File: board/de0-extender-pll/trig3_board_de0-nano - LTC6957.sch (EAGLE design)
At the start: 94 parts, among them IC1 FT230XQ, J12 4p-2.54, J13 BU-SMB-V, J17 2p-2.54, J23 2p-2.54, J24 2p-2.54, J32 2p-2.54, J34 2p-2.54, J38 2p-2.54, J42 2p-2.54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

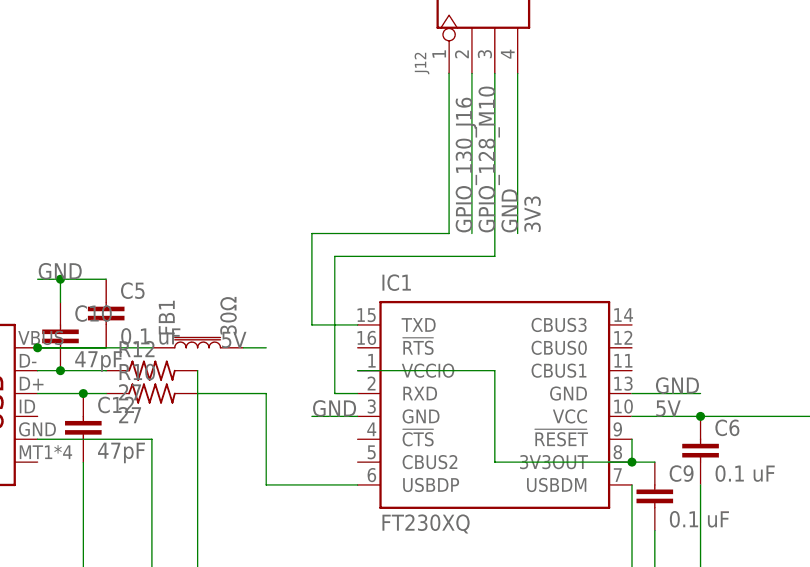
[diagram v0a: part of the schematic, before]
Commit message: rotated footprints and cosmetic updates to board
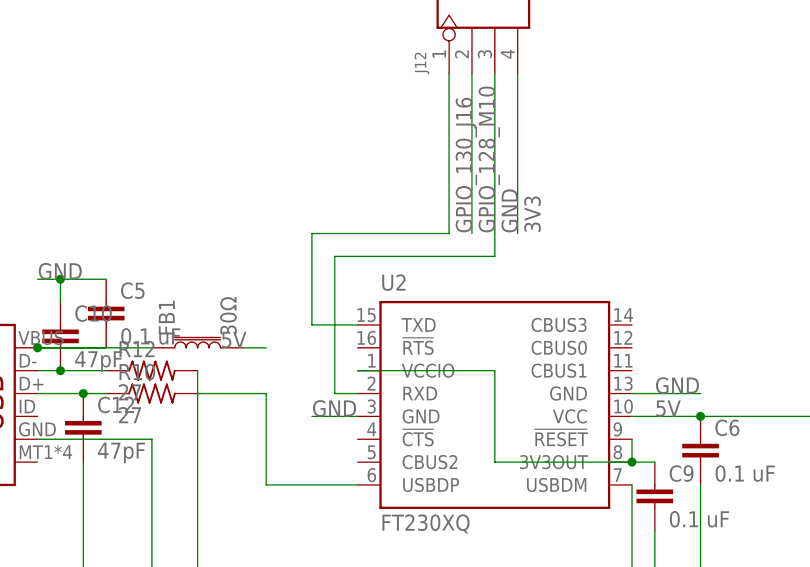
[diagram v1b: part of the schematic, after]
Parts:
- removed IC1: FT230XQ, ftdichip:FT230XQ
- added U2: FT230XQ, ftdichip-rotate-footprint-jlcpcb:FT230XQ
- renumbered VSLUE5 to U5, VSLUE7 to U4, VSLUE9 to U3
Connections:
- net 5V: now also U2.VCC; no longer IC1.VCC
- net GND: now also U2.GND, U2.GND@1, U2.RXD; no longer IC1.GND, IC1.GND@1, IC1.RXD
- net GPIO_130_J16: now also U2.TXD; no longer IC1.TXD
- net N$12: now also U2.USBDP; no longer IC1.USBDP
- net N$13: now also U2.USBDM; no longer IC1.USBDM
- net N$14: now also U2.!RESET, U2.3V3OUT, U2.VCCIO; no longer IC1.!RESET, IC1.3V3OUT, IC1.VCCIO

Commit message: ready for ordering
will probably need to do one last check
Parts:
- A6, B6, C11, C16, CLK-IN+, CLK-IN-, CLK_OUT+, CLK_OUT-, E11, E7, F9, J13, K15P, K16N, L15_R11P, L16_R11N, N11, P11, P15, P16_R15N, P9, R13P, R16_R15P, T13N: LCSC_PART# (none) -> C496549
- C13: LCSC_PART# (none) -> C19666
- J1: value (none) -> USB micro-b
- LED1: device led:LEDCHIP-LED0805 -> led:LEDSML0805
- S2: LCSC_PART# (none) -> C2842669

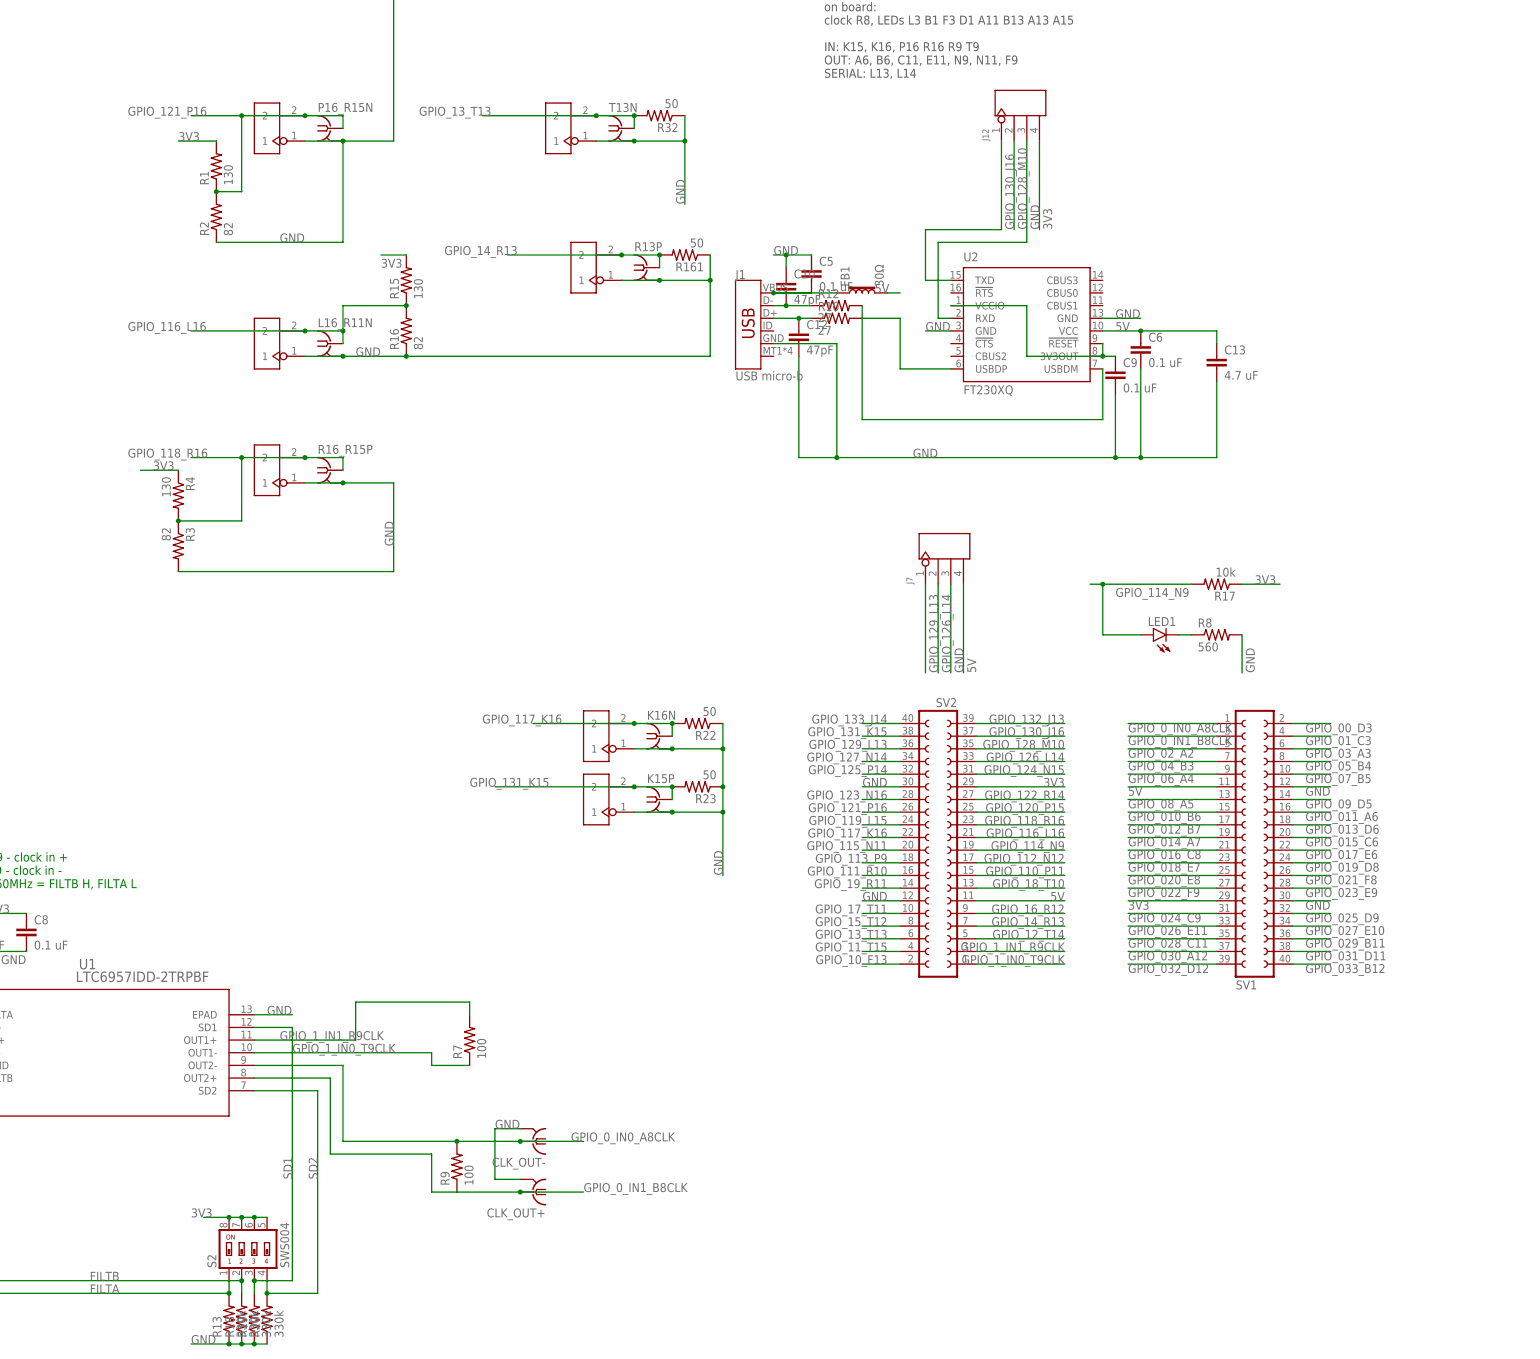
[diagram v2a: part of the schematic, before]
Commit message: fixed usb connection error; changed connector; change dip switch part
added sd1, sd2, filta, filtb to gpio pins also
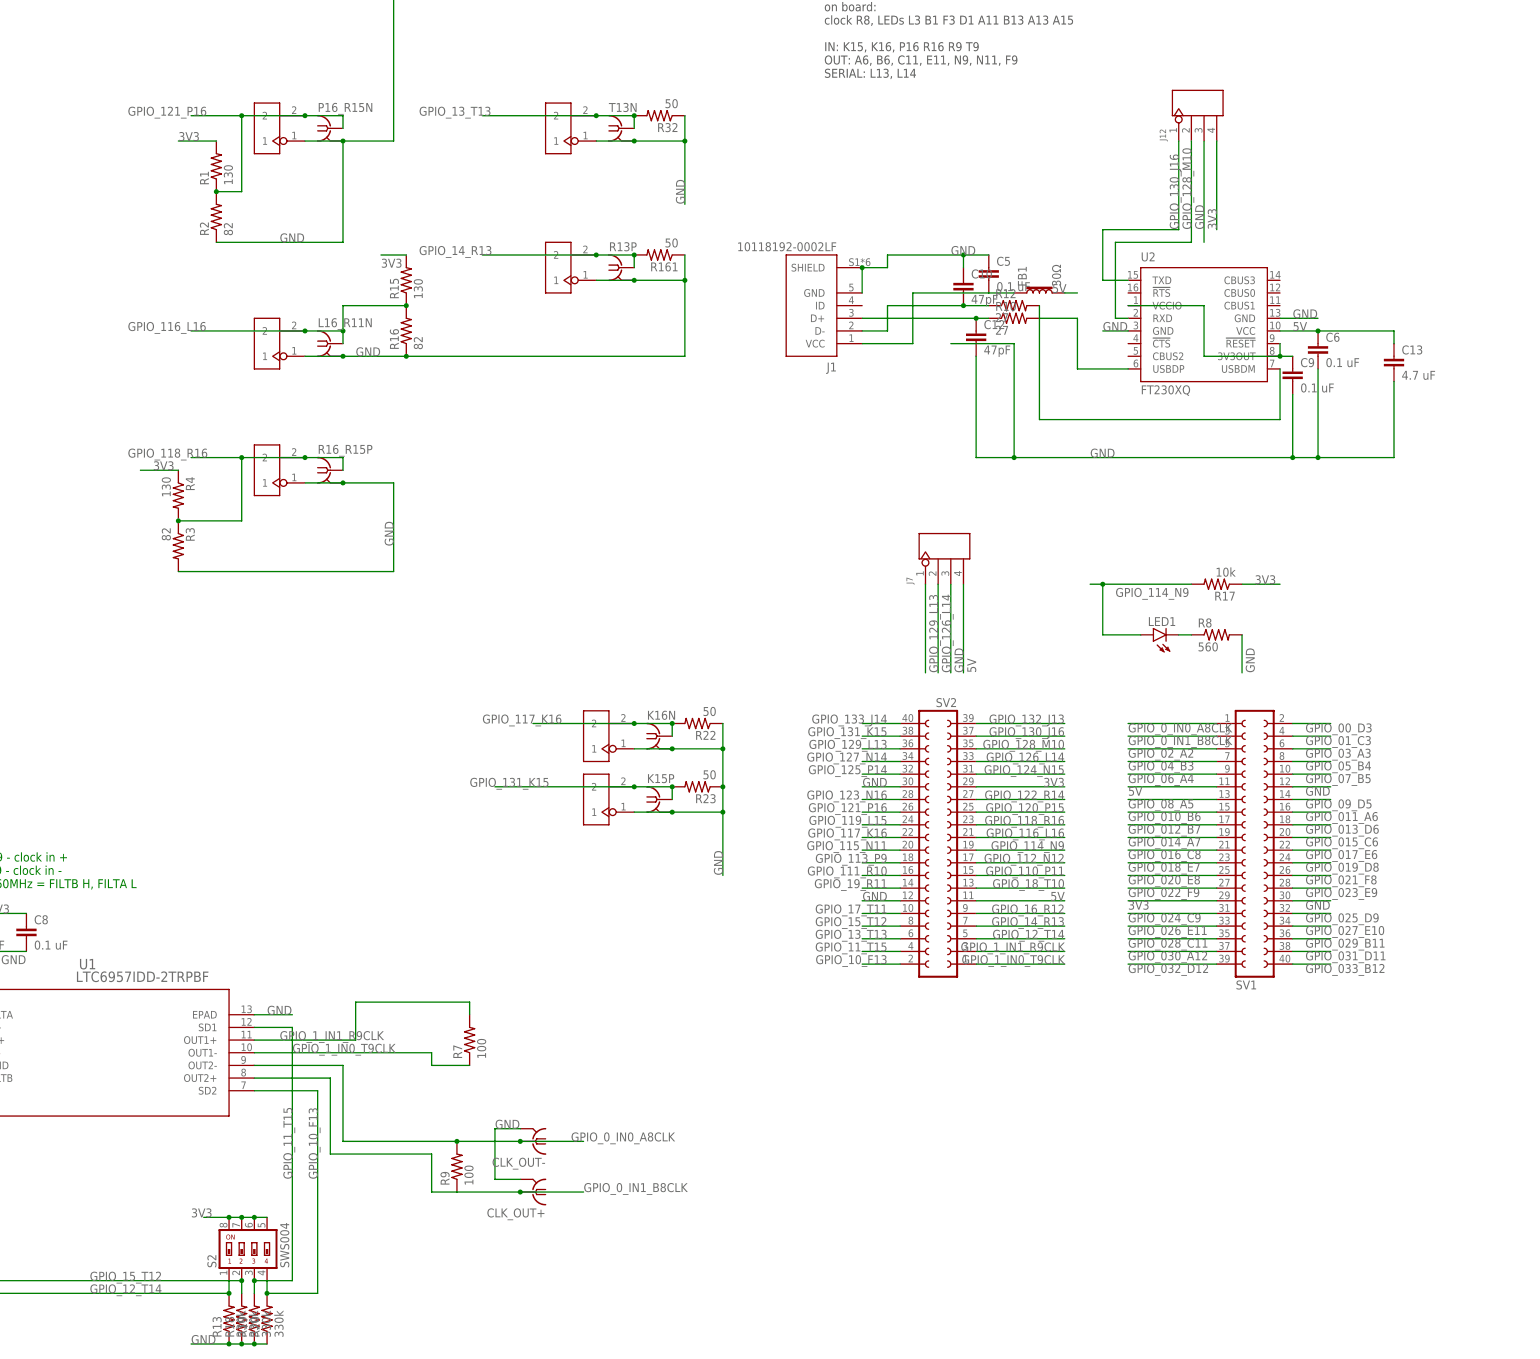
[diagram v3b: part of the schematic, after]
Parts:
- J1: value USB micro-b -> 10118192-0002LF; device SparkFun-Connectors:USB_MICRO-B_SMT -> 10118192-0002LF:10118192-0002LF; LCSC_PART# C2926993 -> C132564
- S2: LCSC_PART# C2842669 -> C221954
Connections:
- removed net FILTA: R13.2, S2.1, U1.FILTA
- removed net FILTB: R18.2, S2.2, U1.FILTB
- removed net SD1: R19.2, S2.3, U1.SD1
- removed net SD2: R20.2, S2.4, U1.SD2
- net GND: now also J1.SHIELD; no longer U2.RXD
- net GPIO_10_F13: now also R20.2, S2.4, U1.SD2
- net GPIO_11_T15: now also R19.2, S2.3, U1.SD1
- net GPIO_128_M10: now also U2.RXD
- net GPIO_12_T14: now also R13.2, S2.1, U1.FILTA
- net GPIO_15_T12: now also R18.2, S2.2, U1.FILTB
- net N$6: now also J1.VCC; no longer J1.VBUS
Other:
- moved on the sheet: C10, C12, C13, C5, C6, C9, FB1, J12, R10, R12, R13P, R161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

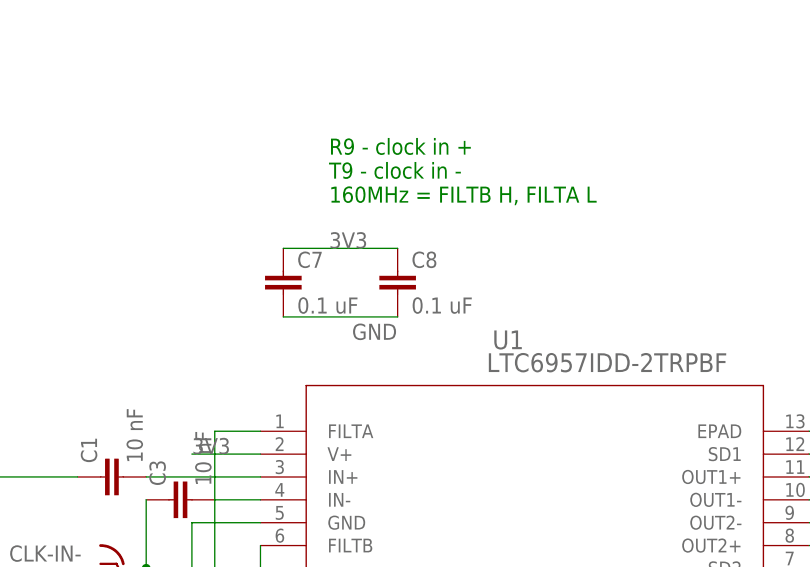
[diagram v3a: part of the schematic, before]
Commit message: one change to silkscreen; added 4.7 uF capacitors to 3.3V header connections
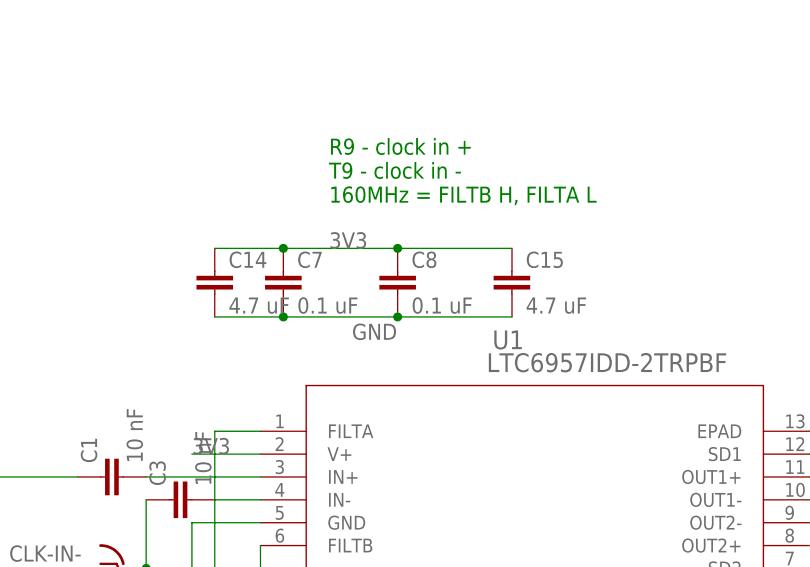
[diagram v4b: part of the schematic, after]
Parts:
- added C14, C15: 4.7 uF, rcl:C-EUC0603
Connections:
- net 3V3: now also C14.1, C15.1
- net GND: now also C14.2, C15.2
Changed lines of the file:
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@@
 <attribute name="LCSC_PART#" value="C132564"/>
+</part>
+<part name="C14" library="rcl" library_urn="urn:adsk.eagle:library:334" deviceset="C-EU" device="C0603" package3d_urn="urn:adsk.eagle:package:23616/2" value="4.7 uF">
+<spice>
+<pinmapping spiceprefix="C">
+<pinmap gate="G$1" pin="1" pinorder="1"/>
+<pinmap gate="G$1" pin="2" pinorder="2"/>
+</pinmapping>
+</spice>
+<attribute name="LCSC_PART#" value="C19666"/>
+</part>
+<part name="C15" library="rcl" library_urn="urn:adsk.eagle:library:334" deviceset="C-EU" device="C0603" package3d_urn="urn:adsk.eagle:package:23616/2" value="4.7 uF">
+<spice>
+<pinmapping spiceprefix="C">
+<pinmap gate="G$1" pin="1" pinorder="1"/>
+<pinmap gate="G$1" pin="2" pinorder="2"/>
+</pinmapping>
+</spice>
+<attribute name="LCSC_PART#" value="C19666"/>
 </part>
 </parts>
@@
 <attribute name="LCSC_PART#" x="30.48" y="175.26" size="1.778" layer="96" rot="R180" display="off"/>
 </instance>
+<instance part="C14" gate="G$1" x="-147.32" y="50.8" smashed="yes">
+<attribute name="NAME" x="-145.796" y="51.181" size="1.778" layer="95"/>
+<attribute name="VALUE" x="-145.796" y="46.101" size="1.778" layer="96"/>
+<attribute name="LCSC_PART#" x="-147.32" y="50.8" size="1.778" layer="96" display="off"/>
+</instance>
+<instance part="C15" gate="G$1" x="-114.3" y="50.8" smashed="yes">
+<attribute name="NAME" x="-112.776" y="51.181" size="1.778" layer="95"/>
+<attribute name="VALUE" x="-112.776" y="46.101" size="1.778" layer="96"/>
+<attribute name="LCSC_PART#" x="-114.3" y="50.8" size="1.778" layer="96" display="off"/>
+</instance>
 </instances>
 <busses>
@@
 <wire x1="-139.7" y1="45.72" x2="-127" y2="45.72" width="0.1524" layer="91"/>
 <label x="-132.08" y="43.18" size="1.778" layer="95"/>
+<pinref part="C14" gate="G$1" pin="2"/>
+<wire x1="-147.32" y1="45.72" x2="-139.7" y2="45.72" width="0.1524" layer="91"/>
+<junction x="-139.7" y="45.72"/>
+<pinref part="C15" gate="G$1" pin="2"/>
+<wire x1="-114.3" y1="45.72" x2="-127" y2="45.72" width="0.1524" layer="91"/>
+<junction x="-127" y="45.72"/>
 </segment>
 <segment>
@@
 <wire x1="-127" y1="53.34" x2="-139.7" y2="53.34" width="0.1524" layer="91"/>
 <label x="-134.62" y="53.34" size="1.778" layer="95"/>
-</segment>
-<segment>
+<pinref part="C14" gate="G$1" pin="1"/>
+<wire x1="-147.32" y1="53.34" x2="-139.7" y2="53.34" width="0.1524" layer="91"/>
+<junction x="-139.7" y="53.34"/>
+<pinref part="C15" gate="G$1" pin="1"/>
+<wire x1="-114.3" y1="53.34" x2="-127" y2="53.34" width="0.1524" layer="91"/>
+<junction x="-127" y="53.34"/>
+</segment>
+<segment>
